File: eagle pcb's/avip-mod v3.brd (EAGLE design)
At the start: 63 x 21 mm, 44 parts, among them J1 0ohm, J2 0ohm, J3 0ohm, J4 0ohm, T1 2N2222SOT23, T2 2N2222SOT23, T3 2N2222SOT23, T4 2N2222SOT23, U1 14m2

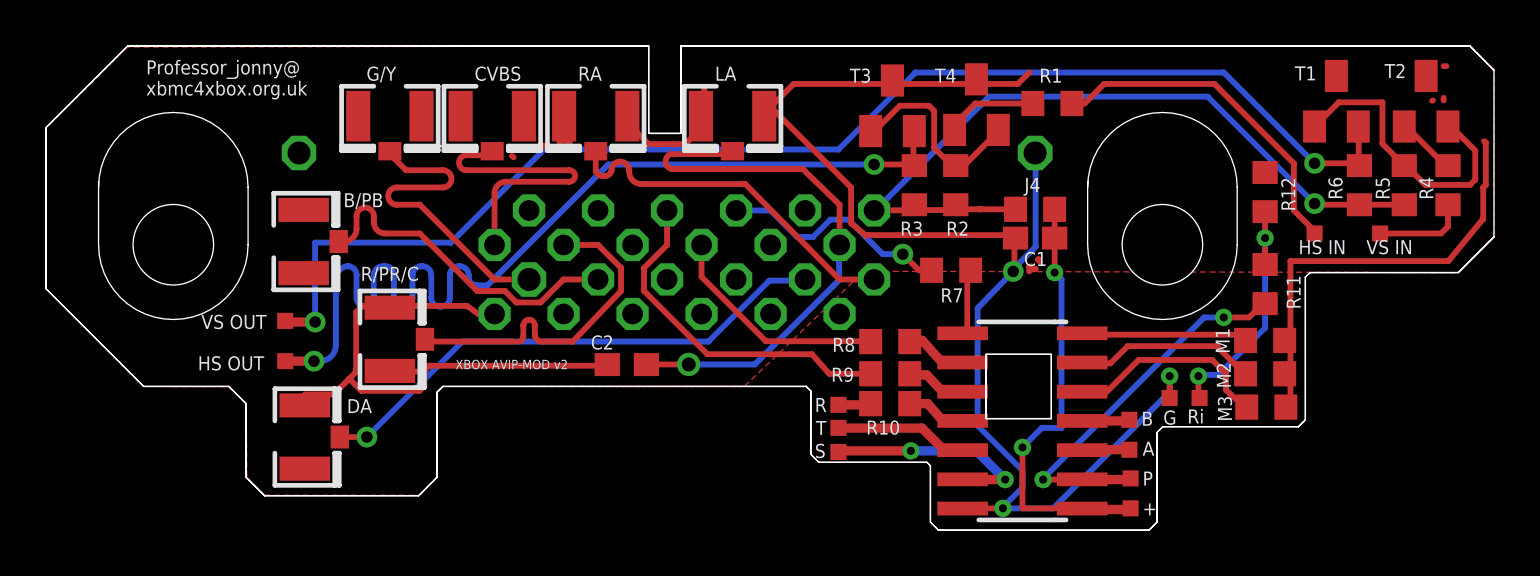
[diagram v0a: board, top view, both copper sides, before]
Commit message: Fix PCB preview and update pictures
Conflict between mill and dimensions layer causing all PCB's to not show up in manufacture preview.
Add pictures of v3, v4 and v4 top PCB.
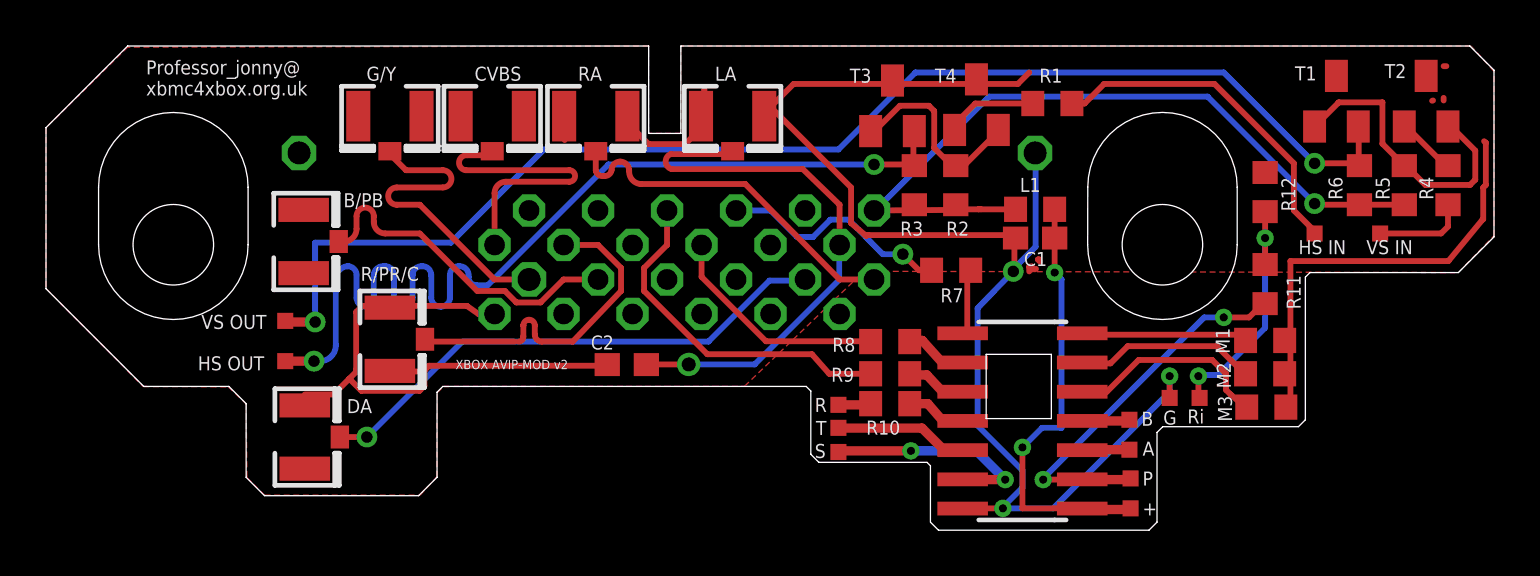
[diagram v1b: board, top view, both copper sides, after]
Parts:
- AVIP: value AVIP -> AVIP1.0-1.5; device XBOX:AVIP -> XBOX:AVIP-1.0-1.5
- renumbered H_SYNC_IN to HS_IN, H_SYNC_OUT to HS_OUT, J4 to L1, PROG to P, RESET to R, RING to RI, SPEAK to S, TOGGLE to T, VCC2 to +, V_SYNC_IN to VS_IN, V_SYNC_OUT to VS_OUT
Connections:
- net GND: now also AVIP.24_VSS; no longer AVIP.24_-VE
- net VCC: now also AVIP.1_VDD; no longer AVIP.1_+VCC
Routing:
- net GND: track 116.3 -> 111.9 mm
